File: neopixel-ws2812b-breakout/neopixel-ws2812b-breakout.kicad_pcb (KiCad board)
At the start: 2 copper layers, 7.6 x 20.3 mm, 4 parts, among them J1 INPUT, J2 OUTPUT

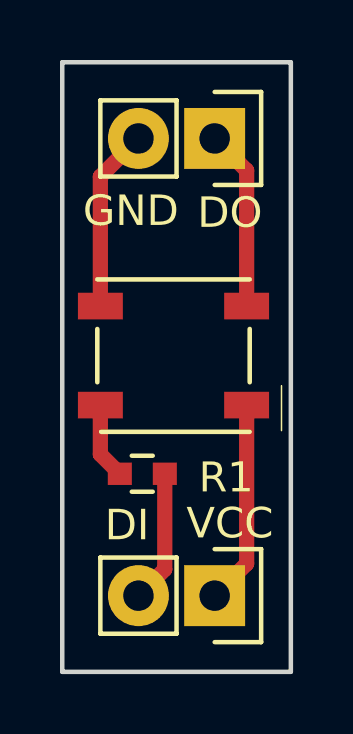
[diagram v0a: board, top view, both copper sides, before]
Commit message: Release Neopixel v1.1. Fixed swapped pads.
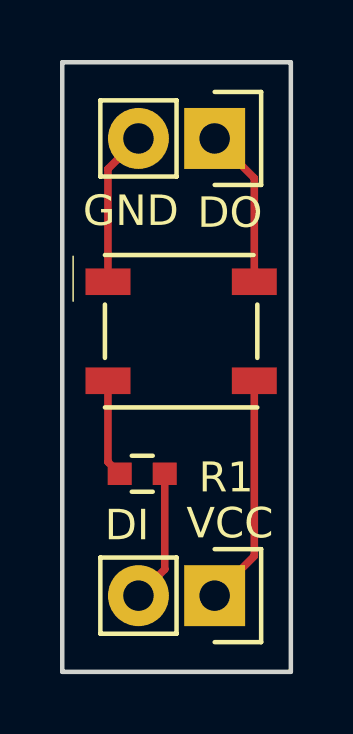
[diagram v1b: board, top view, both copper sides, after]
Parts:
- moved LED1 0.85 mm to (148.7, 102.9), turned to 180 degrees
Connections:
- LED1 pad 1: /VCC -> GND
- LED1 pad 2: /DO -> Net-(LED1-Pad2)
- LED1 pad 3: GND -> /VCC
- LED1 pad 4: Net-(LED1-Pad4) -> /DO
- R1 pad 2: Net-(LED1-Pad4) -> Net-(LED1-Pad2)
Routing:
- net Net-(LED1-Pad2): track 0.00 -> 3.26 mm
- net Net-(LED1-Pad4): track 2.55 -> 0.00 mm
- net /VCC: track 6.79 -> 7.71 mm
- net GND: track 6.11 -> 5.20 mm
- net /DO: track 6.03 -> 5.32 mm
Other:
- board text added: "2/7/17"
- board text added: "RGB5050 Neopixel Breakout v1.1"
- board text removed: "9/1/16"
- board text removed: "RGB5050 Neopixel Breakout v1.0"
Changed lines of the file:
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@@
-(kicad_pcb (version 4) (host pcbnew 4.0.4+e1-6308~48~ubuntu14.04.1-stable)
+(kicad_pcb (version 4) (host pcbnew 4.0.5-e0-6337~49~ubuntu16.04.1)
   (general
-    (links 0)
-    (no_connects 0)
-    (area 104.572999 74.854999 178.510001 123.265001)
+    (links 5)
+    (no_connects 3)
+    (area 144.704999 93.904999 152.475001 114.375001)
     (thickness 1.6)
-    (drawings 17)
-    (tracks 0)
+    (drawings 15)
+    (tracks 10)
     (zones 0)
-    (modules 0)
-    (nets 1)
+    (modules 4)
+    (nets 6)
   )
   (page USLetter)
@@
     (title "Neopixel WS2812B Breakout Board")
     (date "1 Sep 2016")
-    (rev "v1.0")
+    (rev v1.0)
     (company "CERN Open Hardware License v1.2")
-    (comment 1 "jenner@wickerbox.net")
-    (comment 2 "http://wickerbox.net")
+    (comment 1 jenner@wickerbox.net)
+    (comment 2 http://wickerbox.net)
     (comment 3 "Wickerbox Electronics")
   )
@@
   )
   (setup
-    (last_trace_width 0.1524)
+    (last_trace_width 0.254)
     (user_trace_width 0.1524)
     (user_trace_width 0.254)
@@
   (net 3 /DI)
   (net 4 GND)
-  (net 5 "Net-(LED1-Pad4)")
+  (net 5 "Net-(LED1-Pad2)")
   (net_class Default "This is the default net class."
     (clearance 0.254)
@@
     (add_net /VCC)
     (add_net GND)
-    (add_net "Net-(LED1-Pad4)")
+    (add_net "Net-(LED1-Pad2)")
   )
   (net_class Power ""
@@
       (net 3 /DI))
     (pad 2 smd rect (at 0.75 0 180) (size 0.8 0.75) (layers F.Cu F.Paste F.Mask)
-      (net 5 "Net-(LED1-Pad4)"))
+      (net 5 "Net-(LED1-Pad2)"))
   )
   (module Wickerlib:LED-RGB-5050-SMD (layer F.Cu)
-    (at 148.4884 103.759)
-    (fp_text reference LED1 (at 0.025 0) (layer F.Fab)
-      (effects (font (size 1 1) (thickness 0.15)))
-    )
-    (fp_text value WS2812B (at 0.025 0.05) (layer F.Fab) hide
-      (effects (font (size 1 1) (thickness 0.15)))
-    )
+    (at 148.7424 102.9462 180)
+    (fp_text reference LED1 (at 0.025 0 180) (layer F.Fab)
+      (effects (font (size 1 1) (thickness 0.15)))
+    )
+    (fp_text value WS2812B (at 0.025 0.05 180) (layer F.Fab) hide
+      (effects (font (size 1 1) (thickness 0.15)))
+    )
+    (fp_line (start 2.413 3.048) (end 3.81 1.143) (layer F.Fab) (width 0.0464))
     (fp_circle (center 2.45 1.65) (end 2.5 1.8) (layer F.Fab) (width 0.05))
     (fp_line (start 3.6 1) (end 3.6 2.5) (layer F.SilkS) (width 0.05))
-    (fp_line (start 3.81 3.048) (end 3.81 -2.921) (layer F.Fab) (width 0.05))
-    (fp_line (start -3.81 3.048) (end 3.81 3.048) (layer F.Fab) (width 0.05))
+    (fp_line (start 3.81 1.143) (end 3.81 -2.921) (layer F.Fab) (width 0.05))
+    (fp_line (start -3.81 3.048) (end 2.413 3.048) (layer F.Fab) (width 0.05))
     (fp_line (start -3.81 -2.921) (end -3.81 3.048) (layer F.Fab) (width 0.05))
     (fp_line (start 3.81 -2.921) (end -3.81 -2.921) (layer F.Fab) (width 0.05))
-    (fp_text user %R (at 0.1 -3.302) (layer F.SilkS) hide
+    (fp_text user %R (at 0.1 -3.302 180) (layer F.SilkS) hide
       (effects (font (size 1 1) (thickness 0.15)))
     )
@@
     (fp_line (start -2.54 -2.54) (end 2.54 -2.54) (layer F.SilkS) (width 0.1524))
     (fp_line (start 2.54 -0.889) (end 2.54 0.889) (layer F.SilkS) (width 0.1524))
-    (pad 1 smd rect (at 2.4384 1.651) (size 1.4986 0.889) (layers F.Cu F.Paste F.Mask)
+    (pad 1 smd rect (at 2.4384 1.651 180) (size 1.4986 0.889) (layers F.Cu F.Paste F.Mask)
+      (net 4 GND))
+    (pad 2 smd rect (at 2.4384 -1.651 180) (size 1.4986 0.889) (layers F.Cu F.Paste F.Mask)
+      (net 5 "Net-(LED1-Pad2)"))
+    (pad 3 smd rect (at -2.4384 -1.651 180) (size 1.4986 0.889) (layers F.Cu F.Paste F.Mask)
       (net 1 /VCC))
-    (pad 2 smd rect (at 2.4384 -1.651) (size 1.4986 0.889) (layers F.Cu F.Paste F.Mask)
+    (pad 4 smd rect (at -2.4384 1.651 180) (size 1.4986 0.889) (layers F.Cu F.Paste F.Mask)
       (net 2 /DO))
-    (pad 3 smd rect (at -2.4384 -1.651) (size 1.4986 0.889) (layers F.Cu F.Paste F.Mask)
-      (net 4 GND))
-    (pad 4 smd rect (at -2.4384 1.651) (size 1.4986 0.889) (layers F.Cu F.Paste F.Mask)
-      (net 5 "Net-(LED1-Pad4)"))
-  )
-  (gr_text 9/1/16 (at 148.59 116.332) (layer F.Fab)
+  )
+  (gr_text 2/7/17 (at 148.59 116.332) (layer F.Fab)
     (effects (font (size 1.27 1.27) (thickness 0.2032)))
   )
-  (gr_text "RGB5050 Neopixel\nBreakout v1.0" (at 149.098 91.186) (layer F.Fab)
+  (gr_text "RGB5050 Neopixel\nBreakout v1.1" (at 149.098 91.186) (layer F.Fab)
     (effects (font (size 1.27 1.27) (thickness 0.2032)))
   )
@@
   (gr_line (start 152.4 114.3) (end 144.78 114.3) (layer Edge.Cuts) (width 0.15))
   (gr_line (start 152.4 93.98) (end 152.4 114.3) (layer Edge.Cuts) (width 0.15))
-  (segment (start 150.9268 105.41) (end 150.9268 110.6932) (width 0.508) (layer F.Cu) (net 1))
-  (segment (start 150.9268 110.6932) (end 149.86 111.76) (width 0.508) (layer F.Cu) (net 1))
-  (segment (start 150.9268 102.108) (end 150.9268 97.5868) (width 0.508) (layer F.Cu) (net 2))
-  (segment (start 150.9268 97.5868) (end 149.86 96.52) (width 0.508) (layer F.Cu) (net 2))
-  (segment (start 148.197 107.696) (end 148.197 110.883) (width 0.508) (layer F.Cu) (net 3))
-  (segment (start 148.197 110.883) (end 147.32 111.76) (width 0.508) (layer F.Cu) (net 3))
-  (segment (start 146.05 102.108) (end 146.05 97.79) (width 0.508) (layer F.Cu) (net 4))
-  (segment (start 146.05 97.79) (end 147.32 96.52) (width 0.508) (layer F.Cu) (net 4))
-  (segment (start 146.05 105.41) (end 146.05 107.049) (width 0.508) (layer F.Cu) (net 5))
-  (segment (start 146.05 107.049) (end 146.697 107.696) (width 0.508) (layer F.Cu) (net 5))
+  (segment (start 151.1808 104.5972) (end 151.1808 110.4392) (width 0.254) (layer F.Cu) (net 1))
+  (segment (start 151.1808 110.4392) (end 149.86 111.76) (width 0.254) (layer F.Cu) (net 1))
+  (segment (start 151.1808 101.2952) (end 151.1808 97.8408) (width 0.254) (layer F.Cu) (net 2))
+  (segment (start 151.1808 97.8408) (end 149.86 96.52) (width 0.254) (layer F.Cu) (net 2))
+  (segment (start 148.197 107.696) (end 148.197 110.883) (width 0.254) (layer F.Cu) (net 3))
+  (segment (start 148.197 110.883) (end 147.32 111.76) (width 0.254) (layer F.Cu) (net 3))
+  (segment (start 146.304 101.2952) (end 146.304 97.536) (width 0.254) (layer F.Cu) (net 4))
+  (segment (start 146.304 97.536) (end 147.32 96.52) (width 0.254) (layer F.Cu) (net 4))
+  (segment (start 146.304 104.5972) (end 146.304 107.303) (width 0.254) (layer F.Cu) (net 5))
+  (segment (start 146.304 107.303) (end 146.697 107.696) (width 0.254) (layer F.Cu) (net 5))
 )
